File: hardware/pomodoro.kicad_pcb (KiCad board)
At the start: 2 copper layers, 57.2 x 57.2 mm, 24 parts, among them IC1 ATMEGA328-P, SW1 RESET, SW2 SW_PUSH, U1 7805, X1 16 MHz

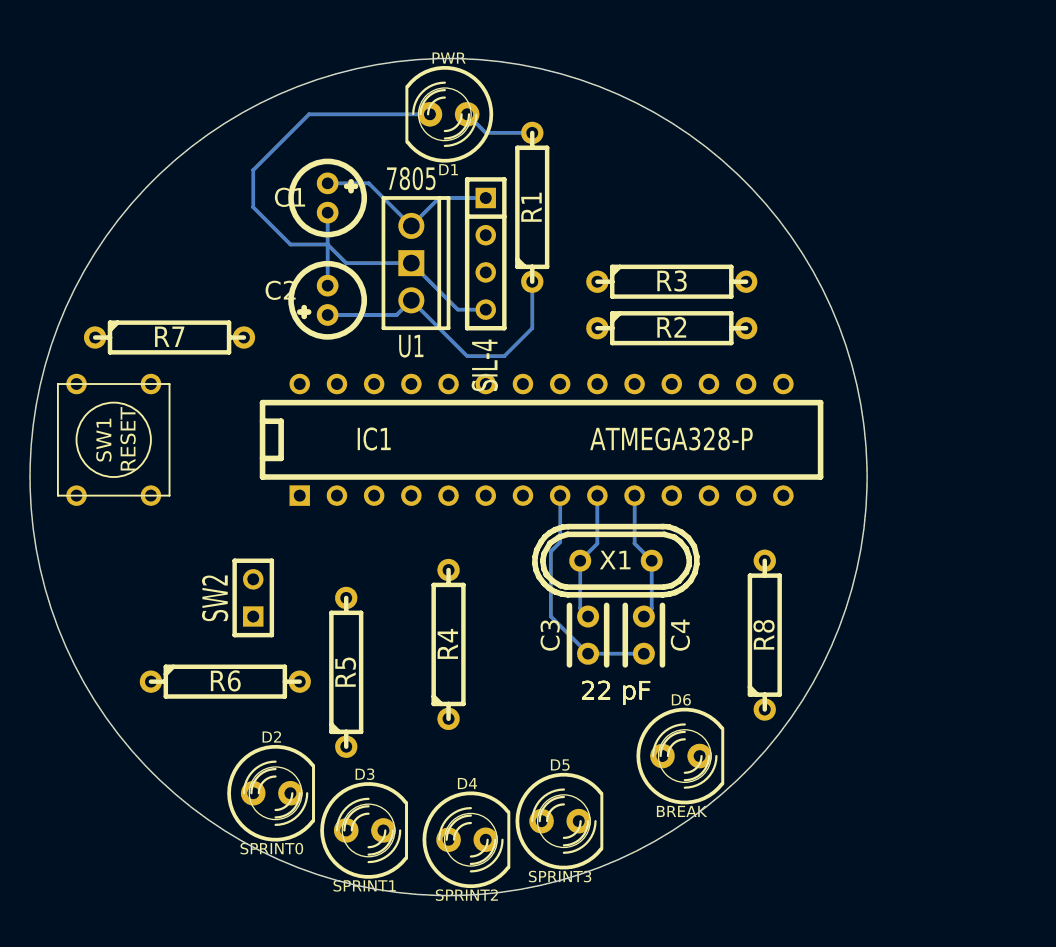
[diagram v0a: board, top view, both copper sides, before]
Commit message: more layout of traces  layout for PSU to ATMega  reset and push button traced
I may move D1, shift the PSU at AVR up, and make room for resistor layout for diodes
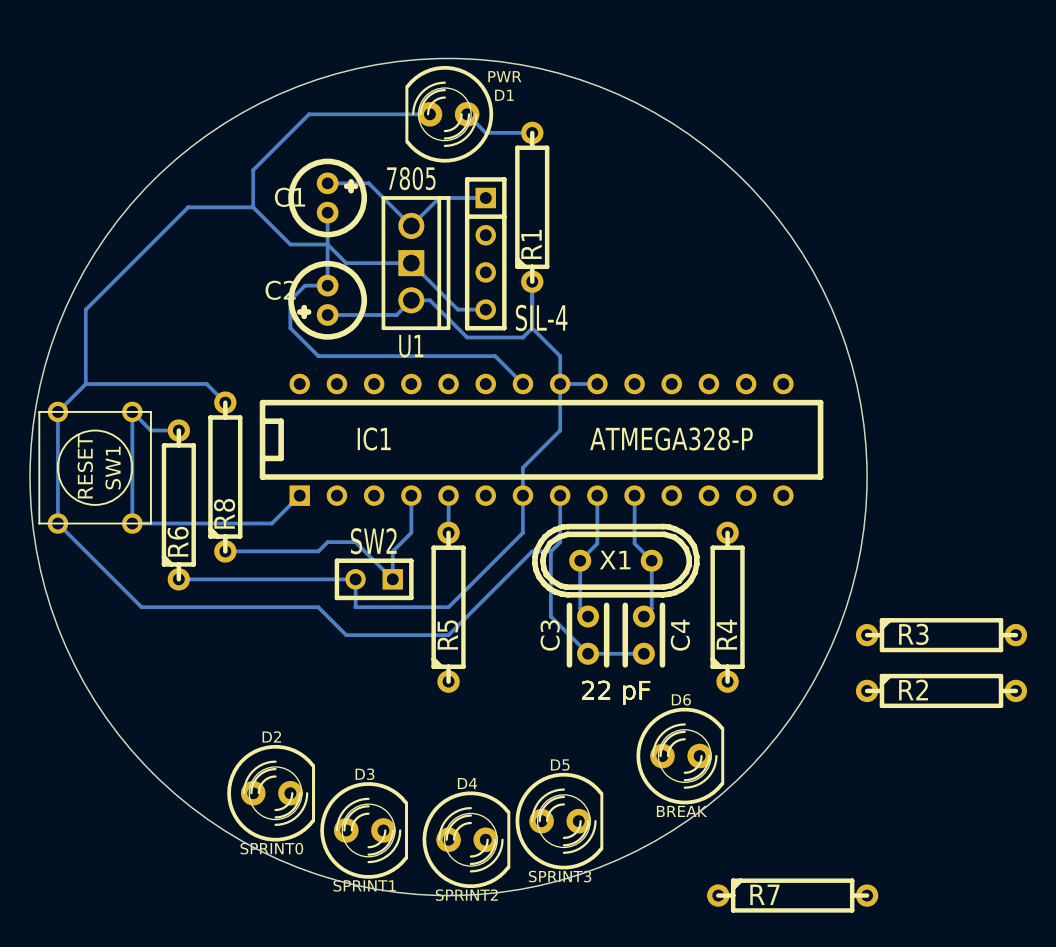
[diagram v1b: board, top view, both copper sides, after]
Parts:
- moved R7 57.1 mm to (172.7, 120.7)
- moved R8 38.4 mm to (134.0, 92.1)
- moved R2 30.9 mm to (182.9, 106.7)
- moved R3 30.4 mm to (182.9, 102.9)
- moved R4 19.2 mm to (168.3, 101.0)
- moved R6 12.5 mm to (130.8, 94.0), turned to 90 degrees
- moved SW2 8.35 mm to (144.1, 99.1), turned to 180 degrees
- moved R5 8.28 mm to (149.2, 101.0)
- moved SW1 2.29 mm to (125.1, 91.4), turned to 270 degrees
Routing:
- net GND: track 56.8 -> 158.0 mm
- net Net-(C2-Pad1): track 19.9 -> 67.9 mm
- net Net-(IC1-Pad1): track 0.00 -> 23.5 mm
- net Net-(IC1-Pad4): track 0.00 -> 19.0 mm
- net Net-(IC1-Pad5): track 0.00 -> 2.54 mm

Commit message: need to reconfigure led output pins
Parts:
- moved R7 19.3 mm to (169.7, 101.6), turned to 90 degrees
- moved R3 15.8 mm to (167.1, 101.6), turned to 90 degrees
- moved R2 11.8 mm to (172.2, 101.6), turned to 90 degrees
- moved D4 10.7 mm to (140.0, 115.1), turned to 180 degrees
- moved D3 10.4 mm to (134.1, 111.8), turned to 180 degrees
- moved D5 10.4 mm to (146.6, 116.8), turned to 180 degrees
- moved D2 10.4 mm to (129.3, 106.9), turned to 180 degrees
- moved C4 9.61 mm to (153.0, 105.4), turned to 0 degrees
- moved D6 9.38 mm to (156.8, 115.6), turned to 180 degrees
- moved C3 6.02 mm to (153.0, 102.2), turned to 0 degrees
- moved X1 5.75 mm to (160.0, 103.5), turned to 90 degrees
- moved R4 3.86 mm to (164.5, 101.6)
- moved R1 3.17 mm to (154.9, 76.8)
- moved D1 2.29 mm to (147.3, 68.6), turned to 270 degrees
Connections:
- D2 pad 2: Net-(D2-Pad2) -> GND
- D3 pad 2: Net-(D3-Pad2) -> GND
- D4 pad 2: Net-(D4-Pad2) -> GND
- D5 pad 2: Net-(D5-Pad2) -> GND
- D6 pad 2: Net-(D6-Pad2) -> GND
- R8 pad 1: Net-(IC1-Pad4) -> GND
- R8 pad 2: GND -> Net-(IC1-Pad4)
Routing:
- net GND: track 158.0 -> 182.5 mm
- net Net-(C4-Pad2): track 8.96 -> 18.5 mm
- net Net-(IC1-Pad4): track 19.0 -> 11.6 mm
- net Net-(C2-Pad1): track 67.9 -> 61.6 mm
- net Net-(D1-Pad1): track 4.97 -> 0.00 mm
- net Net-(C3-Pad2): track 8.96 -> 12.9 mm
- net Net-(IC1-Pad5): track 2.54 -> 0.00 mm

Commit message: some knucklehead didnt retrace the LED he moved
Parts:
- moved D1 2.70 mm to (149.4, 66.8)
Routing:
- net GND: track 182.5 -> 200.3 mm
- net Net-(D1-Pad1): track 0.00 -> 10.5 mm

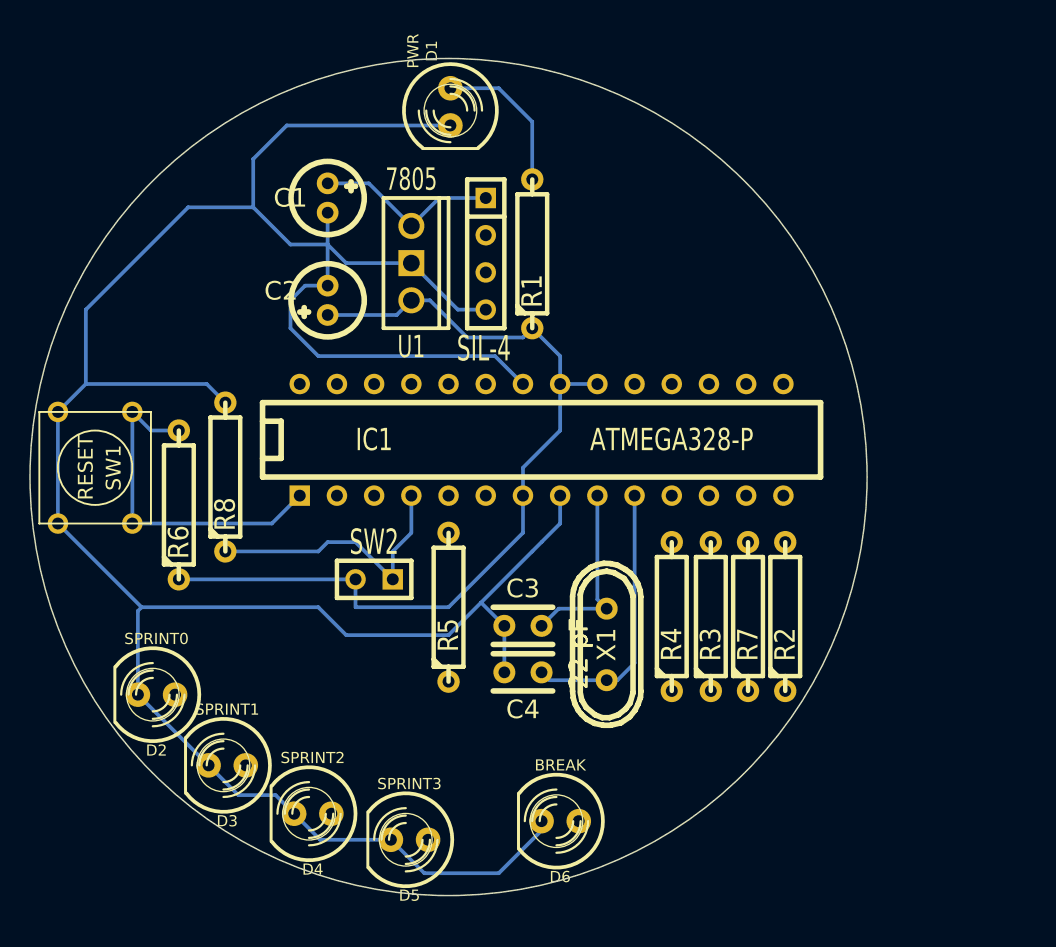
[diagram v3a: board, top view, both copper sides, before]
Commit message: looks like everything is placed and connected on PCB. need to add mounting holes and a diagram for the parts to manufacture
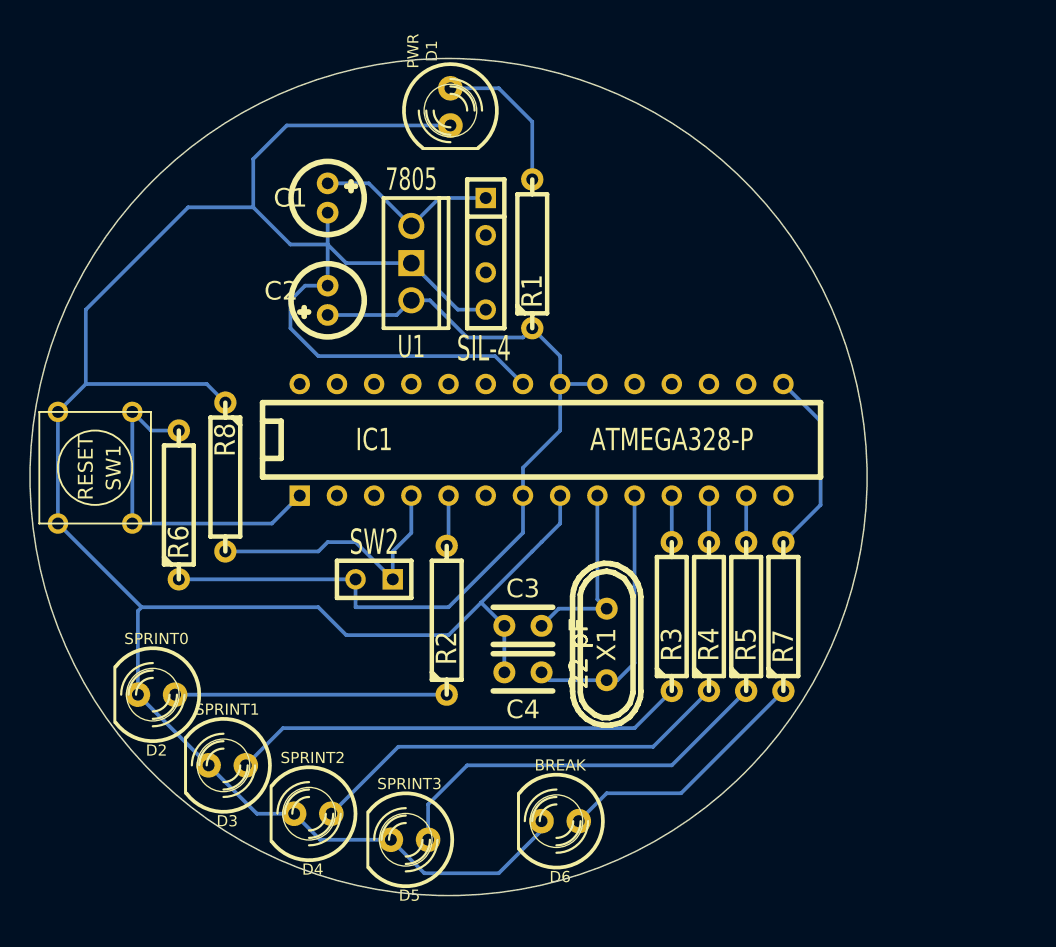
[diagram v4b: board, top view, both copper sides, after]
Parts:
- moved R2 23.1 mm to (149.1, 101.9)
- moved R5 20.3 mm to (169.5, 101.6)
- moved R3 2.67 mm to (164.5, 101.6)
- moved R4 2.54 mm to (167.0, 101.6)
- moved R7 2.41 mm to (172.1, 101.6)
- turned R8 to 270 degrees
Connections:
- R2 pad 2: Net-(IC1-Pad15) -> Net-(IC1-Pad5)
- R3 pad 2: Net-(IC1-Pad12) -> Net-(IC1-Pad11)
- R4 pad 2: Net-(IC1-Pad11) -> Net-(IC1-Pad12)
- R5 pad 2: Net-(IC1-Pad5) -> Net-(IC1-Pad13)
- R7 pad 2: Net-(IC1-Pad13) -> Net-(IC1-Pad15)
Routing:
- net Net-(D3-Pad1): track 0.00 -> 31.2 mm
- net Net-(D4-Pad1): track 0.00 -> 29.3 mm
- net Net-(D5-Pad1): track 0.00 -> 27.3 mm
- net Net-(D2-Pad1): track 0.00 -> 18.5 mm
- net Net-(D6-Pad1): track 0.00 -> 17.7 mm
- net Net-(IC1-Pad15): track 0.00 -> 12.9 mm
- net GND: track 200.3 -> 192.9 mm
- net Net-(IC1-Pad4): track 11.6 -> 19.0 mm
- net Net-(IC1-Pad5): track 0.00 -> 3.48 mm
- net Net-(IC1-Pad13): track 0.00 -> 3.17 mm
- net Net-(IC1-Pad12): track 0.00 -> 3.17 mm
- net Net-(IC1-Pad11): track 0.00 -> 3.17 mm

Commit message: Added mounting holes to PCB and moved traces
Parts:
- added MH: MountingHole_3mm_RevA_Date21Jun2010, Mounting_Holes:MountingHole_3mm, F.Cu at (149.4, 117.1)
- added MH: MountingHole_3mm_RevA_Date21Jun2010, Mounting_Holes:MountingHole_3mm, F.Cu at (131.4, 74.3)
- added MH: MountingHole_3mm_RevA_Date21Jun2010, Mounting_Holes:MountingHole_3mm, F.Cu at (167.0, 74.3)
- moved D3 3.95 mm to (131.3, 109.0), turned to 270 degrees
- moved D5 3.89 mm to (142.7, 116.1), turned to 270 degrees
- moved D4 3.75 mm to (136.7, 113.3), turned to 270 degrees
- moved D2 3.53 mm to (127.5, 103.9)
- moved D6 1.02 mm to (156.0, 116.1)
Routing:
- net GND: track 192.9 -> 187.5 mm
- net Net-(D3-Pad1): track 31.2 -> 34.6 mm
- net Net-(D4-Pad1): track 29.3 -> 32.6 mm
- net Net-(D2-Pad1): track 18.5 -> 21.6 mm
- net Net-(D5-Pad1): track 27.3 -> 30.2 mm
- net Net-(D6-Pad1): track 17.7 -> 18.8 mm

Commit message: fixed power led resistor value
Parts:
- R1: value 10K -> 220
